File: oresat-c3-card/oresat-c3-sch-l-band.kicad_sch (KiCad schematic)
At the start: 75 parts, among them U15 Qorvo 856930, U16 AT86RF215, U17 SI4112-GM, U2 BP0805A1308, U23 NCS2-62+, U3 BP0805A1308, U4 BGB741L7ESD, U41 TQP3M9036, U5 BP0805A1308, U7 MAC-24+, X1 TXETALSANF-26.000000

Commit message: Updating BOM and switching to oresat-passive footprints. Fixed some power cutoff limits, and fixed another DC voltage leverl on an LNA!
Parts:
- C142, C49, C8, C9, L11, L2, L22, L3, L4, L5, L6, U2, U3, U4, U5: DST Digi-Key -> DigiKey
- R10, R2, R7, R8, R9: footprint Resistor_SMD:R_0603_1608Metric -> oresat-passives:0603-C-NOSILK; DST Digi-Key -> DigiKey
- R22, R25: DPN (none) -> RMCF0603ZT0R00CT-ND; DST (none) -> DigiKey; MFR Stackpole Electronics Inc -> Stackpole Electronics; MPN (none) -> RMCF0603ZT0R00
- R5: DST (none) -> DigiKey; MFR Stackpole Electronics Inc -> Stackpole Electronics
- R6: DPN (none) -> RMCF0603FT75R0CT-ND; DST (none) -> DigiKey; MPN (none) -> RMCF1206FT75R0
- SH1: DPN (none) -> 903-1212-1-ND; DST (none) -> DigiKey; MFR (none) -> Laird Technologies EMI; MPN (none) -> BMI-S-209-F
- U16, X1: DST (none) -> DigiKey
- U23: DPN 3157-NCS2-62+TR-ND -> 139-NCS2-62; DST (none) -> Mouser
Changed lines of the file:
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@@
 			)
 		)
-		(property "DST" "Digi-Key"
+		(property "DST" "DigiKey"
 			(at 179.07 55.88 0)
 			(effects
@@
 			)
 		)
-		(property "DST" "Digi-Key"
+		(property "DST" "DigiKey"
 			(at 341.63 60.96 0)
 			(effects
@@
 			)
 		)
-		(property "Footprint" "Resistor_SMD:R_0603_1608Metric"
+		(property "Footprint" "oresat-passives:0603-C-NOSILK"
 			(at 266.7 200.66 0)
 			(effects
@@
 			)
 		)
-		(property "Datasheet" "~"
+		(property "Datasheet" "https://www.seielect.com/catalog/SEI-RMCF_RMCP.pdf"
 			(at 266.7 200.66 0)
 			(effects
@@
 			)
 		)
-		(property "DST" "Digi-Key"
+		(property "DST" "DigiKey"
 			(at 266.7 200.66 0)
 			(effects
@@
 			)
 		)
-		(property "DST" "Digi-Key"
+		(property "DST" "DigiKey"
 			(at 196.85 55.88 0)
 			(effects
@@
 			)
 		)
-		(property "MFR" "Stackpole Electronics Inc"
+		(property "MFR" "Stackpole Electronics"
 			(at 113.03 118.11 90)
 			(effects
@@
 			)
 		)
+		(property "DST" "DigiKey"
+			(at 113.03 118.11 90)
+			(effects
+				(font
+					(size 1.27 1.27)
+				)
+				(hide yes)
+			)
+		)
 		(pin "1"
 		)
@@
 			)
 		)
-		(property "Description" ""
+		(property "Description" "75 Ohms ±1% 0.1W, 1/10W Chip Resistor 0603 (1608 Metric) Automotive AEC-Q200 Thick Film"
 			(at 143.51 231.14 0)
 			(effects
@@
 			)
 		)
-		(property "DPN" ""
+		(property "DPN" "RMCF0603FT75R0CT-ND"
 			(at 143.51 231.14 90)
 			(effects
@@
 			)
 		)
-		(property "MPN" ""
+		(property "MPN" "RMCF1206FT75R0"
+			(at 143.51 231.14 90)
+			(effects
+				(font
+					(size 1.27 1.27)
+				)
+				(hide yes)
+			)
+		)
+		(property "DST" "DigiKey"
 			(at 143.51 231.14 90)
 			(effects
@@
 			)
 		)
-		(property "DST" "Digi-Key"
+		(property "DST" "DigiKey"
 			(at 247.65 140.97 0)
 			(effects
@@
 			)
 		)
-		(property "DST" "Digi-Key"
+		(property "DST" "DigiKey"
 			(at 166.37 41.91 0)
 			(effects
@@
 			)
 		)
-		(property "Description" "6 pin ballun with two grounds and an NC."
+		(property "Description" "Signal Conditioning RF XFMR / SURF MOUNT / RoHS"
 			(at 201.93 130.302 0)
 			(effects
@@
 			)
 		)
-		(property "DPN" "3157-NCS2-62+TR-ND"
+		(property "DPN" "139-NCS2-62"
 			(at 201.93 146.05 0)
 			(effects
@@
 			)
 		)
+		(property "DST" "Mouser"
+			(at 201.93 146.05 0)
+			(effects
+				(font
+					(size 1.27 1.27)
+				)
+				(hide yes)
+			)
+		)
 		(pin "5"
 		)
@@
 			)
 		)
-		(property "Datasheet" "~"
+		(property "Datasheet" "https://www.laird.com/document/pmbu-doc-000012068"
 			(at 257.81 104.14 0)
 			(effects
@@
 			)
 		)
-		(property "Description" "Two-piece EMI RF shielding cabinet"
+		(property "Description" "RF Shield Frame 0.728\" (18.50mm) X 1.156\" (29.36mm) Surface Mount"
+			(at 257.81 101.6 0)
+			(effects
+				(font
+					(size 1.27 1.27)
+				)
+				(hide yes)
+			)
+		)
+		(property "DPN" "903-1212-1-ND"
+			(at 257.81 101.6 0)
+			(effects
+				(font
+					(size 1.27 1.27)
+				)
+				(hide yes)
+			)
+		)
+		(property "DST" "DigiKey"
+			(at 257.81 101.6 0)
+			(effects
+				(font
+					(size 1.27 1.27)
+				)
+				(hide yes)
+			)
+		)
+		(property "MFR" "Laird Technologies EMI"
+			(at 257.81 101.6 0)
+			(effects
+				(font
+					(size 1.27 1.27)
+				)
+				(hide yes)
+			)
+		)
+		(property "MPN" "BMI-S-209-F"
 			(at 257.81 101.6 0)
 			(effects
@@
 			)
 		)
-		(property "DST" "Digi-Key"
+		(property "DST" "DigiKey"
 			(at 246.38 60.96 0)
 			(effects
@@
 			)
 		)
-		(property "DST" "Digi-Key"
+		(property "DST" "DigiKey"
 			(at 257.81 140.97 0)
 			(effects
@@
 			)
 		)
-		(property "Description" ""
+		(property "Description" "0 Ohms Jumper Chip Resistor 0603 (1608 Metric) Automotive AEC-Q200 Thick Film"
 			(at 130.81 175.26 0)
 			(effects
@@
 			)
 		)
-		(property "DPN" ""
+		(property "DPN" "RMCF0603ZT0R00CT-ND"
 			(at 130.81 175.26 90)
 			(effects
@@
 			)
 		)
-		(property "MFR" "Stackpole Electronics Inc"
+		(property "MFR" "Stackpole Electronics"
 			(at 130.81 175.26 90)
 			(effects
@@
 			)
 		)
-		(property "MPN" ""
+		(property "MPN" "RMCF0603ZT0R00"
+			(at 130.81 175.26 90)
+			(effects
+				(font
+					(size 1.27 1.27)
+				)
+				(hide yes)
+			)
+		)
+		(property "DST" "DigiKey"
 			(at 130.81 175.26 90)
 			(effects
@@
 			)
 		)
-		(property "Footprint" "Resistor_SMD:R_0603_1608Metric"
+		(property "Footprint" "oresat-passives:0603-C-NOSILK"
 			(at 279.4 193.04 0)
 			(effects
@@
 			)
 		)
-		(property "Datasheet" "~"
+		(property "Datasheet" "https://www.seielect.com/catalog/SEI-RMCF_RMCP.pdf"
 			(at 279.4 193.04 0)
 			(effects
@@
 			)
 		)
-		(property "DST" "Digi-Key"
+		(property "DST" "DigiKey"
 			(at 279.4 193.04 0)
 			(effects
@@
 			)
 		)
-		(property "Description" "AT86RF215-ZUR"
+		(property "Description" "IC RF TxRx Only 802.15.4, General ISM < 1GHz 389.5MHz ~ 510MHz, 779MHz ~ 1.02GHz, 2.4GHz 48-VFQFN Exposed Pad"
 			(at 157.48 149.86 0)
 			(effects
@@
 			)
 		)
+		(property "DST" "DigiKey"
+			(at 157.48 149.86 0)
+			(effects
+				(font
+					(size 1.27 1.27)
+				)
+				(hide yes)
+			)
+		)
 		(pin "8"
 		)
@@
 			)
 		)
-		(property "DST" "Digi-Key"
+		(property "DST" "DigiKey"
 			(at 212.09 57.15 0)
 			(effects
@@
 			)
 		)
-		(property "DST" "Digi-Key"
+		(property "DST" "DigiKey"
 			(at 328.93 144.78 0)
 			(effects
@@
 			)
 		)
-		(property "DST" "Digi-Key"
+		(property "DST" "DigiKey"
 			(at 138.43 60.96 0)
 			(effects
@@
 			)
 		)
-		(property "DST" "Digi-Key"
+		(property "DST" "DigiKey"
 			(at 321.31 185.42 0)
 			(effects
@@
 			)
 		)
+		(property "DST" "DigiKey"
+			(at 100.33 172.72 0)
+			(effects
+				(font
+					(size 1.27 1.27)
+				)
+				(hide yes)
+			)
+		)
 		(pin "3"
 		)
@@
 			)
 		)
-		(property "DST" "Digi-Key"
+		(property "DST" "DigiKey"
 			(at 292.1 53.34 0)
 			(effects
@@
 			)
 		)
-		(property "Footprint" "Resistor_SMD:R_0603_1608Metric"
+		(property "Footprint" "oresat-passives:0603-C-NOSILK"
 			(at 271.78 200.66 0)
 			(effects
@@
 			)
 		)
-		(property "Datasheet" "~"
+		(property "Datasheet" "https://www.seielect.com/catalog/SEI-RMCF_RMCP.pdf"
 			(at 271.78 200.66 0)
 			(effects
@@
 			)
 		)
-		(property "DST" "Digi-Key"
+		(property "DST" "DigiKey"
 			(at 271.78 200.66 0)
 			(effects
@@
 			)
 		)
-		(property "Description" ""
+		(property "Description" "0 Ohms Jumper Chip Resistor 0603 (1608 Metric) Automotive AEC-Q200 Thick Film"
 			(at 130.81 172.72 0)
 			(effects
@@
 			)
 		)
-		(property "DPN" ""
+		(property "DPN" "RMCF0603ZT0R00CT-ND"
 			(at 130.81 172.72 90)
 			(effects
@@
 			)
 		)
-		(property "MFR" "Stackpole Electronics Inc"
+		(property "MFR" "Stackpole Electronics"
+			(at 130.81 172.72 90)
+			(effects
+				(font
+					(size 1.27 1.27)
+				)
+				(hide yes)
+			)
+		)
+		(property "MPN" "RMCF0603ZT0R00"
 			(at 130.81 172.72 90)
 			(effects
@@
 			)
 		)
-		(property "MPN" ""
+		(property "DST" "DigiKey"
 			(at 130.81 172.72 90)
 			(effects
@@
 			)
 		)
-		(property "Footprint" "Resistor_SMD:R_0603_1608Metric"
+		(property "Footprint" "oresat-passives:0603-C-NOSILK"
 			(at 185.42 39.37 0)
 			(effects
@@
 			)
 		)
-		(property "Datasheet" "~"
+		(property "Datasheet" "https://www.seielect.com/catalog/SEI-RMCF_RMCP.pdf"
 			(at 185.42 39.37 0)
 			(effects
@@
 			)
 		)
-		(property "DST" "Digi-Key"
+		(property "DST" "DigiKey"
 			(at 185.42 39.37 0)
 			(effects
@@
 			)
 		)
-		(property "DST" "Digi-Key"
+		(property "DST" "DigiKey"
 			(at 274.32 48.26 0)
 			(effects
@@
 			)
 		)
-		(property "Footprint" "Resistor_SMD:R_0603_1608Metric"
+		(property "Footprint" "oresat-passives:0603-C-NOSILK"
 			(at 261.62 200.66 0)
 			(effects
@@
 			)
 		)
-		(property "Datasheet" "~"
+		(property "Datasheet" "https://www.seielect.com/catalog/SEI-RMCF_RMCP.pdf"
 			(at 261.62 200.66 0)
 			(effects
@@
 			)
 		)
-		(property "DST" "Digi-Key"
+		(property "DST" "DigiKey"
 			(at 261.62 200.66 0)
 			(effects
@@
 			)
 		)
-		(property "DST" "Digi-Key"
+		(property "DST" "DigiKey"
 			(at 360.68 144.78 0)
 			(effects
@@
 			)
 		)
-		(property "DST" "Digi-Key"
+		(property "DST" "DigiKey"
 			(at 331.47 213.36 0)
 			(effects

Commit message: All footprints updated. Passes ERC/DRC.
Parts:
- C1, C11, C2: footprint Capacitor_SMD:C_0402_1005Metric -> oresat-passives:0402-B-NOSILK; DPN 399-17374-1-ND -> 399-15987-1-ND; DST Digi-Key -> DigiKey; MPN C0402C220J5GACAUTO -> C0603C220J1GACAUTO
- C12, C143, C144, C145, C37, C38, C4, C41, C42, C54, C9: footprint Capacitor_SMD:C_0402_1005Metric -> oresat-passives:0402-B-NOSILK
- C142, C49, C8: footprint Capacitor_SMD:C_0603_1608Metric -> oresat-passives:0603-C-NOSILK; DPN 587-3473-1-ND -> 490-GRT188R71E105KE13DCT-ND; MFR Taiyo Yuden -> Murata Electronics; MPN TMK107BJ105KAHT -> GRT188R71E105KE13D
- C3: footprint Capacitor_SMD:C_0603_1608Metric -> oresat-passives:0603-C-NOSILK; DPN 587-6374-1-ND -> 399-6820-1-ND; DST Digi-Key -> DigiKey; MFR Taiyo Yuden -> KEMET; MPN UMK107B7473KAHT -> C0603C473K5RACAUTO
- C39, C43, C44, C45, C81, C82, C88, C91, C92: DPN 399-6853-1-ND -> 399-6856-1-ND; DST (none) -> DigiKey; MPN C0603C104J5RACAUTO -> C0603C104K5RACAUTO
- C40: DPN 399-17595-1-ND -> 399-6896-1-ND; DST (none) -> DigiKey; MPN C0603C472J5RACAUTO -> C0603C472K5RACAUTO
- C50, C51: footprint Capacitor_SMD:C_0603_1608Metric -> oresat-passives:0603-C-NOSILK

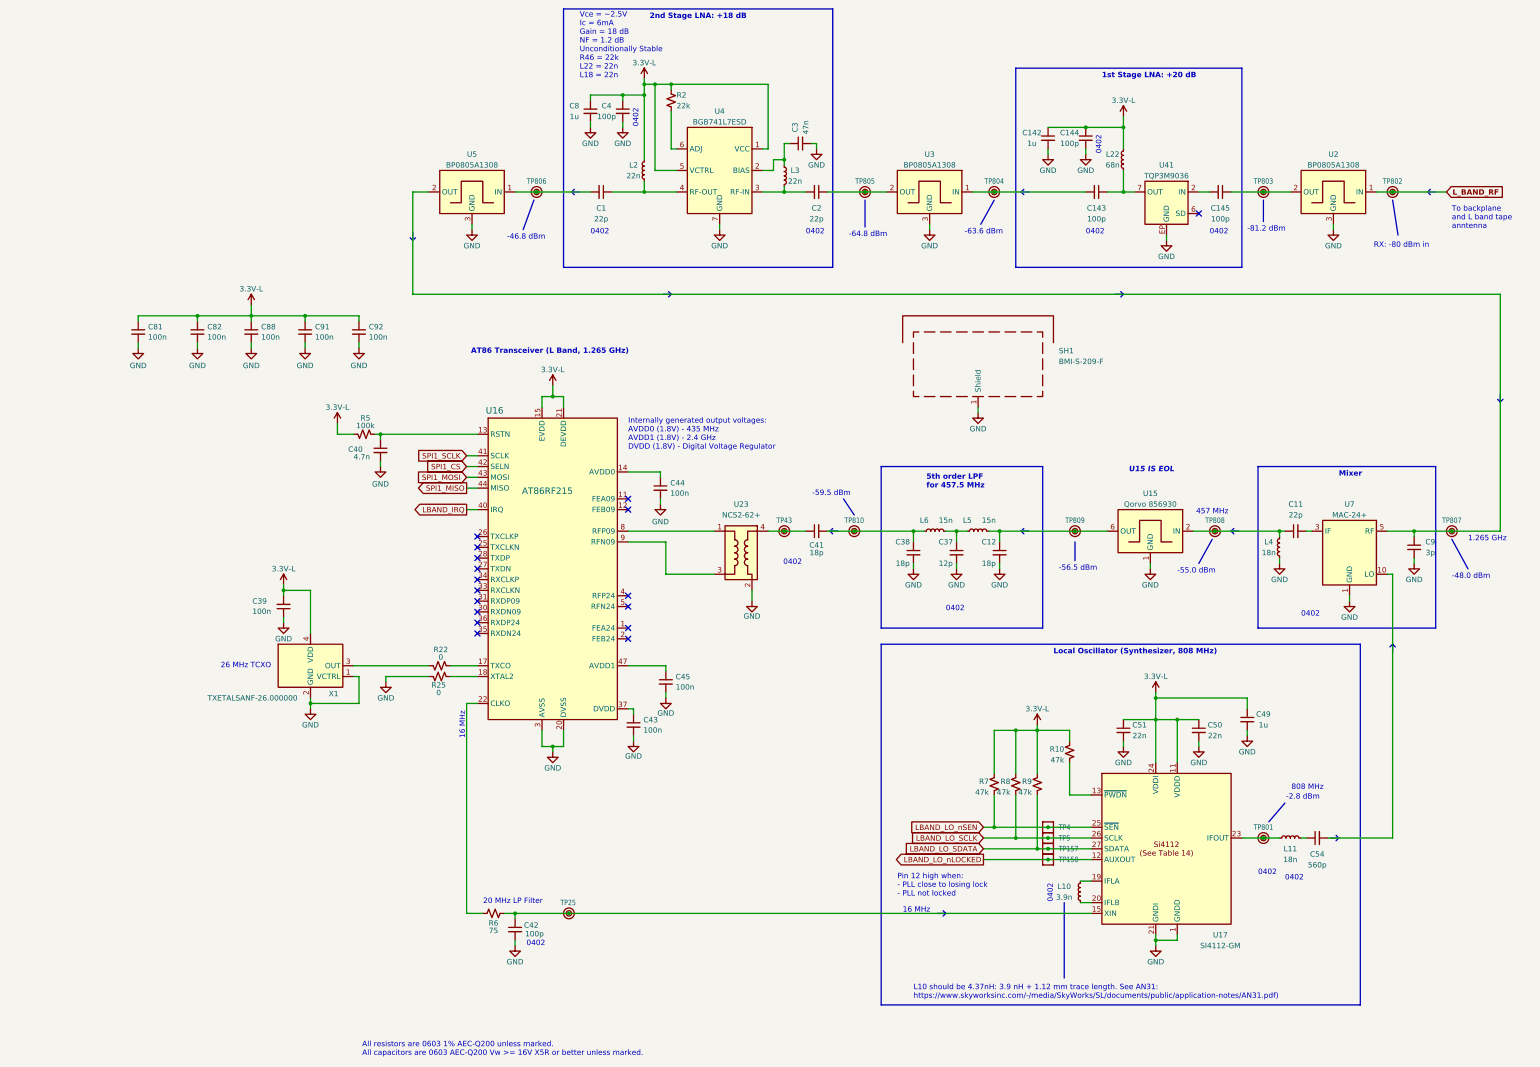
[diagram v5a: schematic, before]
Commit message: All DRC exclusing RF traces are cleaned up.  RF traces cleaned up with mask and bends. Some more notes in the schematic for future us.
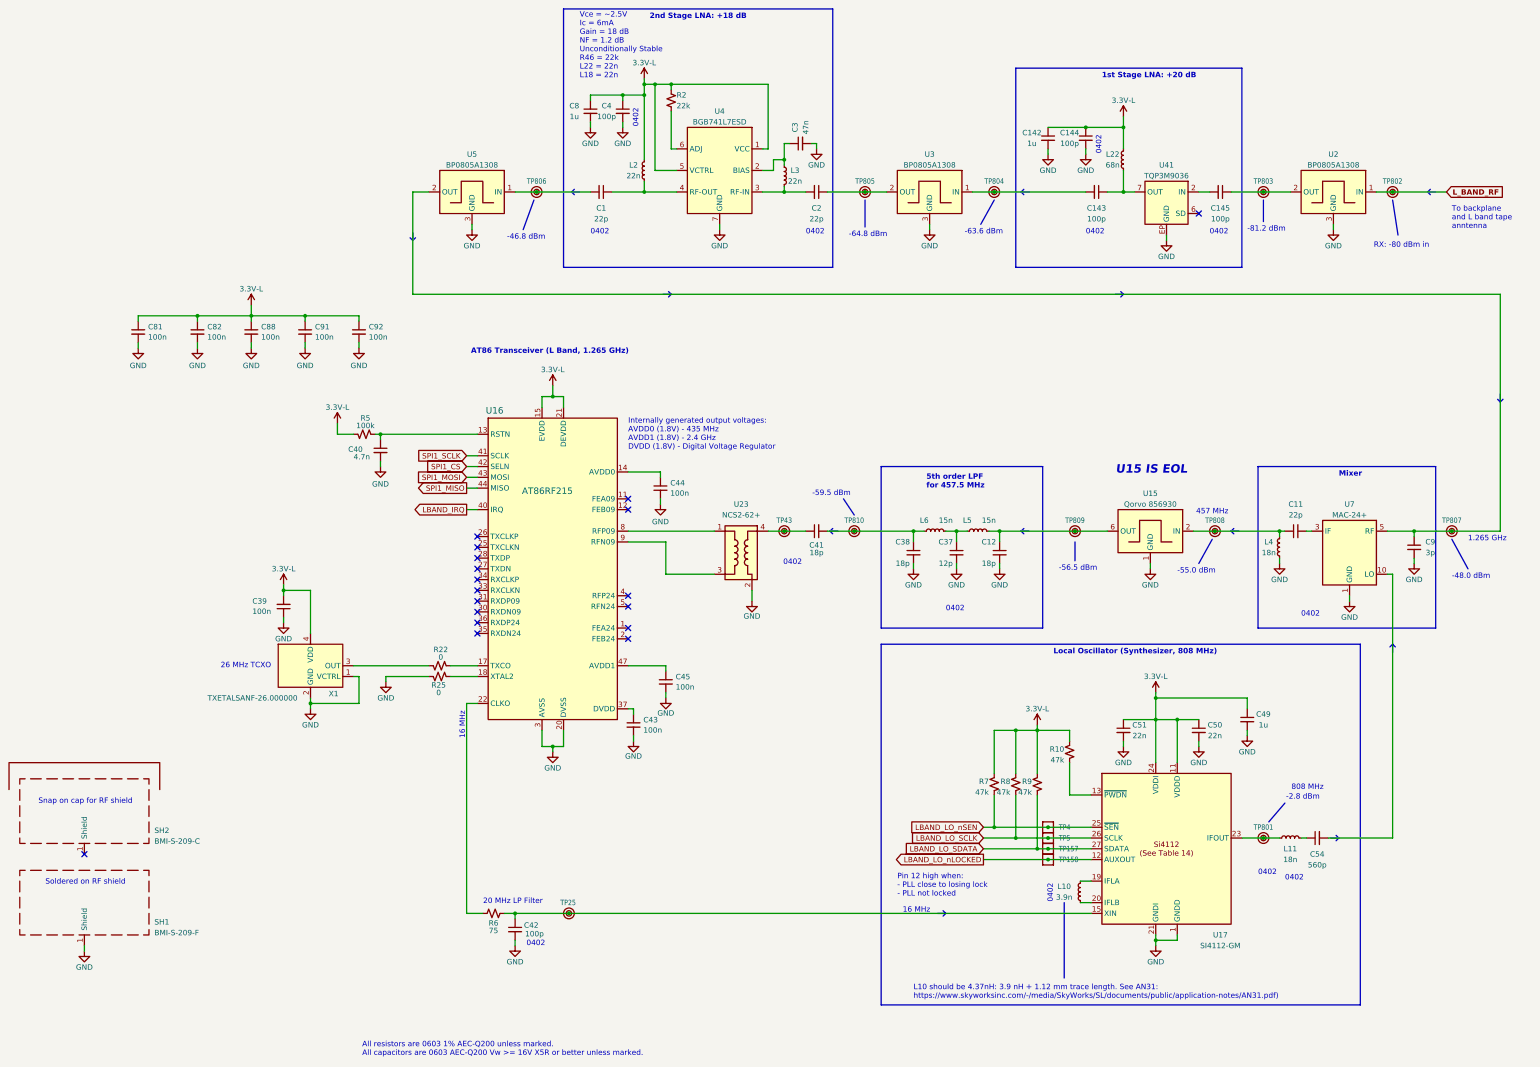
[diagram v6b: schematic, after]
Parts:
- added SH2: BMI-S-209-C, symbol Device:RFShield_TwoPieces
- SH1: symbol Device:RFShield_TwoPieces -> Device:RFShield_OnePiece
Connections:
- no-connect marks 17 -> 18
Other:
- note added: "Snap on cap for RF shield"
- note added: "Soldered on RF shield"
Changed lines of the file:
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@@
 			(font
 				(face "KiCad Font")
-				(size 1.27 1.27)
+				(size 2 2)
 				(thickness 0.254)
 				(bold yes)
@@
 		)
 	)
+	(text "Snap on cap for RF shield"
+		(exclude_from_sim no)
+		(at 47.244 204.724 0)
+		(effects
+			(font
+				(size 1.27 1.27)
+			)
+		)
+	)
 	(text "0402"
 		(exclude_from_sim no)
@@
 		)
 	)
+	(text "Soldered on RF shield\n"
+		(exclude_from_sim no)
+		(at 47.244 223.774 0)
+		(effects
+			(font
+				(size 1.27 1.27)
+			)
+		)
+	)
 	(text "0402"
 		(exclude_from_sim no)
@@
 	)
 	(no_connect
+		(at 46.99 217.17)
+	)
+	(no_connect
 		(at 139.7 165.1)
 	)
@@
 	(wire
 		(pts
-			(xy 257.81 113.03) (xy 257.81 111.76)
+			(xy 46.99 240.03) (xy 46.99 238.76)
 		)
 		(stroke
@@
 	)
 	(symbol
+		(lib_id "Device:RFShield_TwoPieces")
+		(at 46.99 207.01 0)
+		(unit 1)
+		(exclude_from_sim no)
+		(in_bom yes)
+		(on_board no)
+		(dnp no)
+		(property "Reference" "SH2"
+			(at 63.5 211.582 0)
+			(effects
+				(font
+					(size 1.27 1.27)
+				)
+				(justify left)
+			)
+		)
+		(property "Value" "BMI-S-209-C"
+			(at 63.5 214.122 0)
+			(effects
+				(font
+					(size 1.27 1.27)
+				)
+				(justify left)
+			)
+		)
+		(property "Footprint" ""
+			(at 46.99 209.55 0)
+			(effects
+				(font
+					(size 1.27 1.27)
+				)
+				(hide yes)
+			)
+		)
+		(property "Datasheet" "https://www.laird.com/document/pmbu-doc-000012068"
+			(at 46.99 209.55 0)
+			(effects
+				(font
+					(size 1.27 1.27)
+				)
+				(hide yes)
+			)
+		)
+		(property "Description" "RF Shield Cover 0.752\" (19.10mm) X 1.180\" (29.96mm) Non-Vented Snap Fit"
+			(at 46.99 207.01 0)
+			(effects
+				(font
+					(size 1.27 1.27)
+				)
+				(hide yes)
+			)
+		)
+		(property "DPN" "903-1185-ND"
+			(at 46.99 207.01 0)
+			(effects
+				(font
+					(size 1.27 1.27)
+				)
+				(hide yes)
+			)
+		)
+		(property "DST" "DigiKey"
+			(at 46.99 207.01 0)
+			(effects
+				(font
+					(size 1.27 1.27)
+				)
+				(hide yes)
+			)
+		)
+		(property "MFR" "Laird Technologies EMI"
+			(at 46.99 207.01 0)
+			(effects
+				(font
+					(size 1.27 1.27)
+				)
+				(hide yes)
+			)
+		)
+		(property "MPN" "BMI-S-209-C"
+			(at 46.99 207.01 0)
+			(effects
+				(font
+					(size 1.27 1.27)
+				)
+				(hide yes)
+			)
+		)
+		(pin "1"
+		)
+		(instances
+			(project ""
+				(path "/65d12cdd-c326-4033-9053-c59fa4e0b25e/1b68ea4b-cacf-4529-b1d4-9be5d7c1043c"
+					(reference "SH2")
+					(unit 1)
+				)
+			)
+		)
+	)
+	(symbol
 		(lib_id "Device:L_Small")
 		(at 179.07 55.88 0)
@@
 	)
 	(symbol
-		(lib_id "Device:RFShield_TwoPieces")
-		(at 257.81 101.6 0)
+		(lib_id "Device:RFShield_OnePiece")
+		(at 46.99 228.6 0)
 		(unit 1)
 		(exclude_from_sim no)
@@
 		(on_board yes)
 		(dnp no)
-		(fields_autoplaced yes)
 		(property "Reference" "SH1"
-			(at 276.86 98.4249 0)
+			(at 63.5 233.172 0)
 			(effects
 				(font
@@
 		)
 		(property "Value" "BMI-S-209-F"
-			(at 276.86 100.9649 0)
+			(at 63.5 235.712 0)
 			(effects
 				(font
@@
 		)
 		(property "Footprint" "RF_Shielding:Laird_Technologies_BMI-S-209-F_29.36x18.50mm"
-			(at 257.81 104.14 0)
+			(at 46.99 231.14 0)
 			(effects
 				(font
@@
 		)
 		(property "Datasheet" "https://www.laird.com/document/pmbu-doc-000012068"
-			(at 257.81 104.14 0)
+			(at 46.99 231.14 0)
 			(effects
 				(font
@@
 		)
 		(property "Description" "RF Shield Frame 0.728\" (18.50mm) X 1.156\" (29.36mm) Surface Mount"
-			(at 257.81 101.6 0)
+			(at 46.99 228.6 0)
 			(effects
 				(font
@@
 		)
 		(property "DPN" "903-1212-1-ND"
-			(at 257.81 101.6 0)
+			(at 46.99 228.6 0)
 			(effects
 				(font
@@
 		)
 		(property "DST" "DigiKey"
-			(at 257.81 101.6 0)
+			(at 46.99 228.6 0)
 			(effects
 				(font
@@
 		)
 		(property "MFR" "Laird Technologies EMI"
-			(at 257.81 101.6 0)
+			(at 46.99 228.6 0)
 			(effects
 				(font
@@
 		)
 		(property "MPN" "BMI-S-209-F"
-			(at 257.81 101.6 0)
+			(at 46.99 228.6 0)
 			(effects
 				(font
@@
 	(symbol
 		(lib_id "power:GND")
-		(at 257.81 113.03 0)
+		(at 46.99 240.03 0)
 		(unit 1)
 		(exclude_from_sim no)
@@
 		(dnp no)
 		(property "Reference" "#PWR017"
-			(at 257.81 119.38 0)
+			(at 46.99 246.38 0)
 			(effects
 				(font
@@
 		)
 		(property "Value" "GND"
-			(at 257.81 116.84 0)
+			(at 46.99 243.84 0)
 			(effects
 				(font
@@
 		)
 		(property "Footprint" ""
-			(at 257.81 113.03 0)
+			(at 46.99 240.03 0)
 			(effects
 				(font
@@
 		)
 		(property "Datasheet" ""
-			(at 257.81 113.03 0)
+			(at 46.99 240.03 0)
 			(effects
 				(font
@@
 		)
 		(property "Description" "Power symbol creates a global label with name \"GND\" , ground"
-			(at 257.81 113.03 0)
+			(at 46.99 240.03 0)
 			(effects
 				(font
